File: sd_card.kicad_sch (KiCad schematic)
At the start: 19 parts, among them J5 Screw_Terminal_01x03, J601 DM3AT-SF-PEJM5_40_, U11 EMIF06-MSD02N16, U602 ADM2565EBRNZ

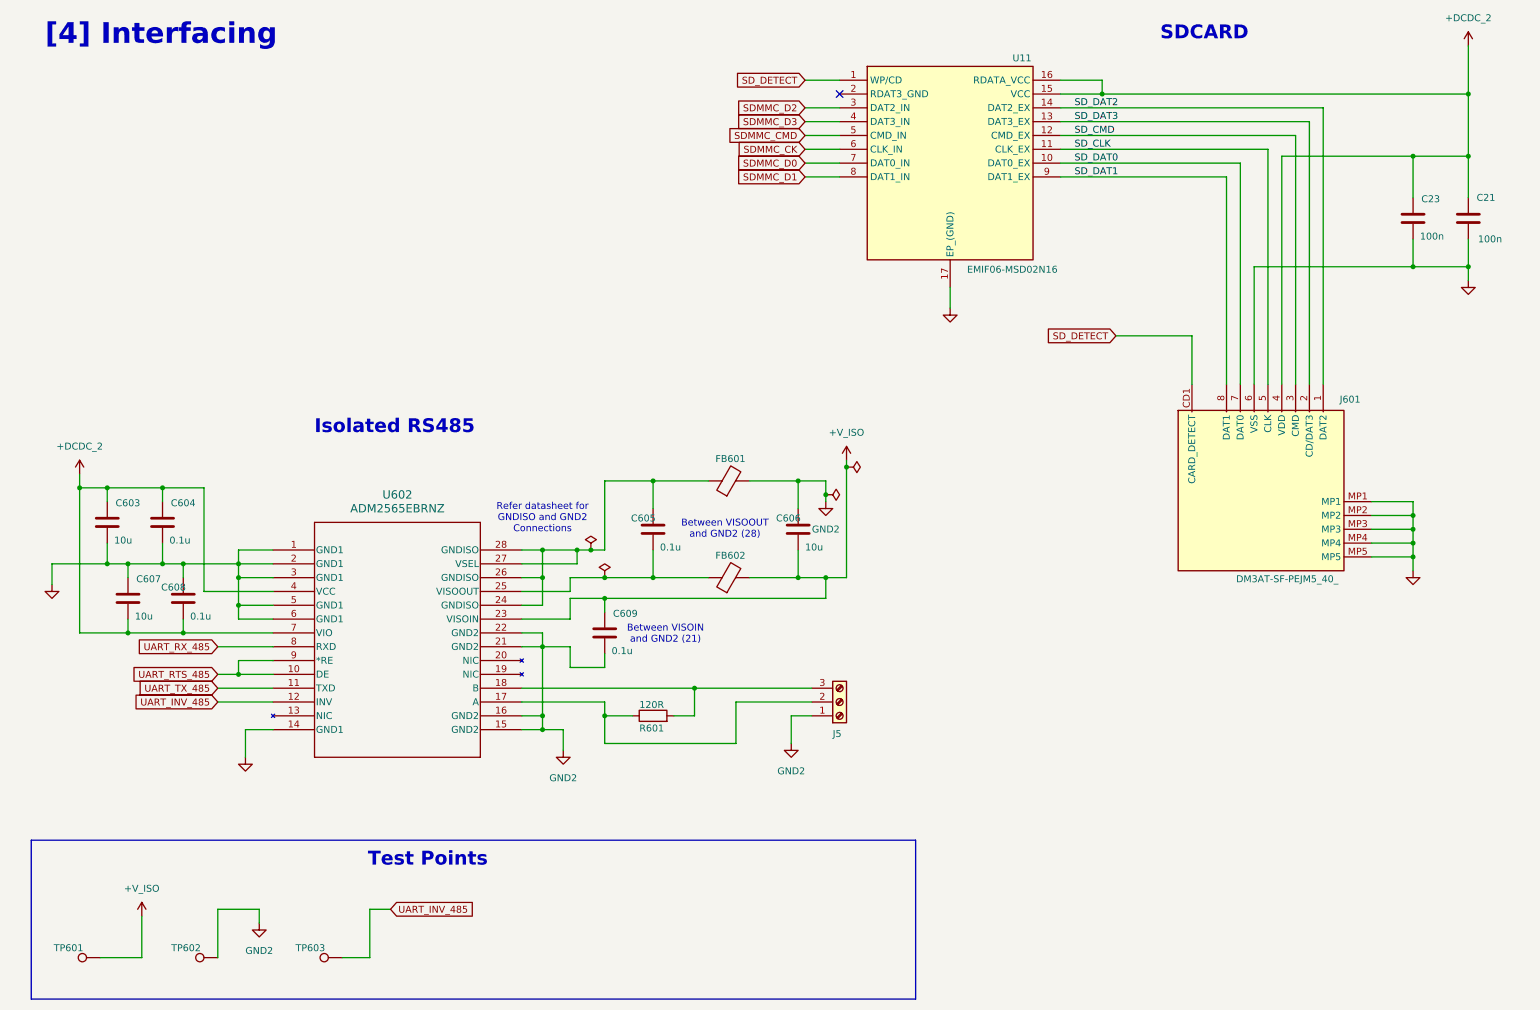
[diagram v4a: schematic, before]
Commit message: v2.0 schematics updated
1. Need to be tested for errors
2. PCB layout is not started yet
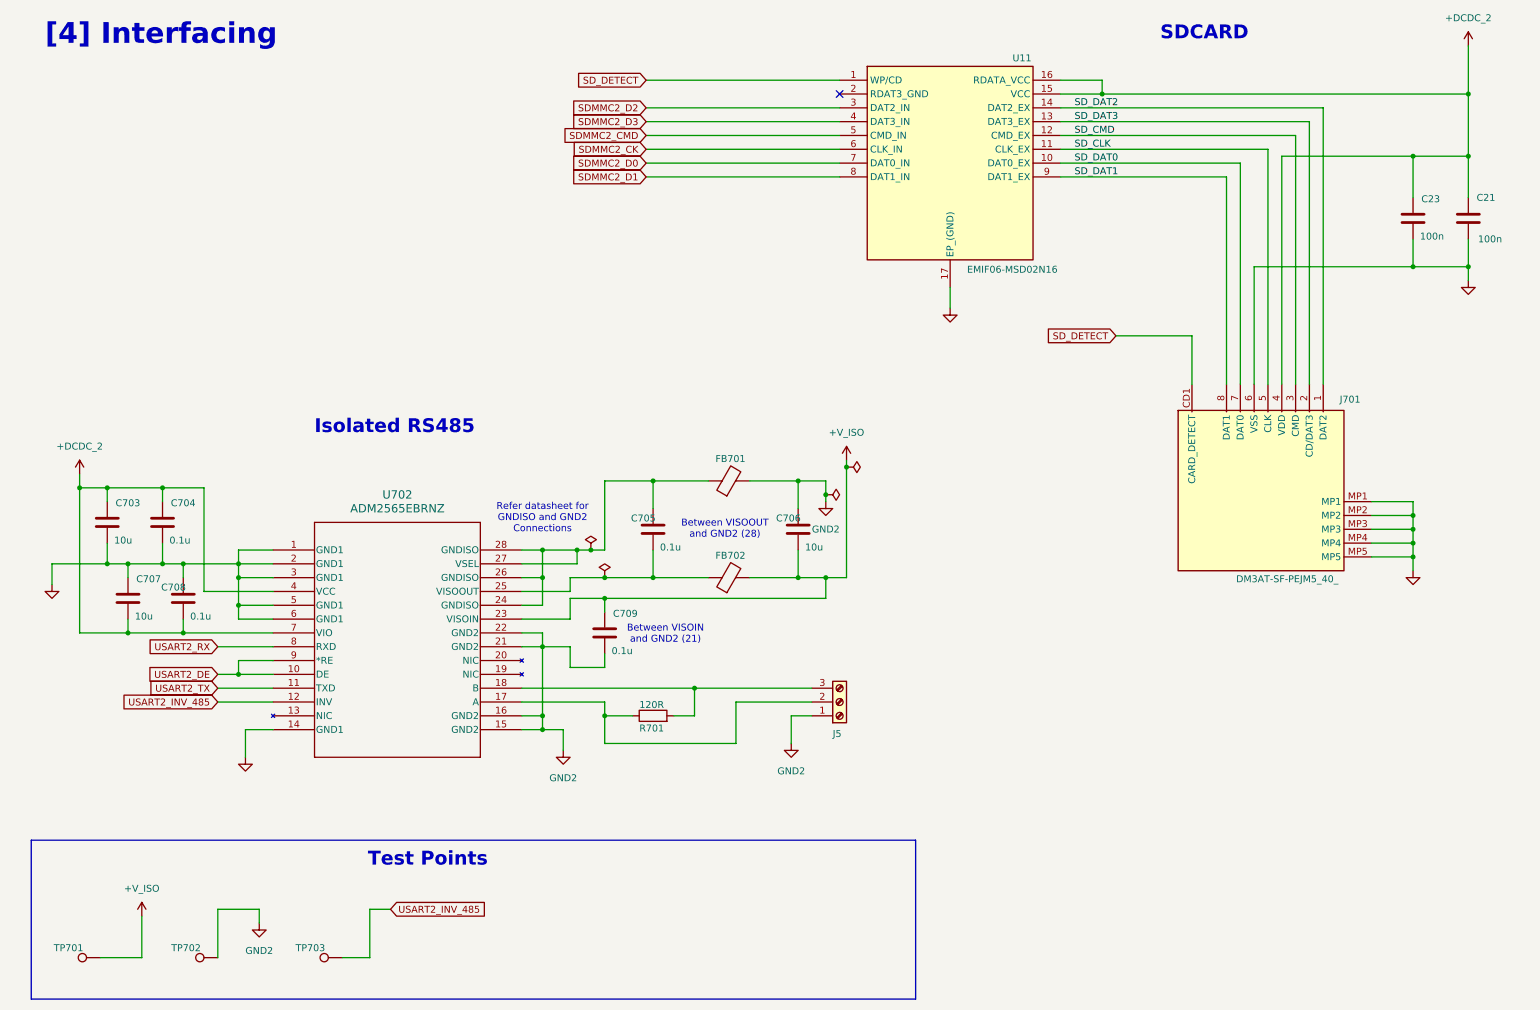
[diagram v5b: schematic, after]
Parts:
- renumbered C603 to C703, C604 to C704, C605 to C705, C606 to C706, C607 to C707, C608 to C708, C609 to C709, FB601 to FB701, FB602 to FB702, J601 to J701, R601 to R701, TP601 to TP701, TP602 to TP702, TP603 to TP703, U602 to U702
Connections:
- net SDMMC_CK renamed SDMMC2_CK
- net SDMMC_CMD renamed SDMMC2_CMD
- net SDMMC_D0 renamed SDMMC2_D0
- net SDMMC_D1 renamed SDMMC2_D1
- net SDMMC_D2 renamed SDMMC2_D2
- net SDMMC_D3 renamed SDMMC2_D3
- net UART_INV_485 renamed USART2_INV_485
- net UART_RTS_485 renamed USART2_DE
- net UART_RX_485 renamed USART2_RX
- net UART_TX_485 renamed USART2_TX

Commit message: minor formatting updates
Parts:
- TP701, TP702, TP703: footprint EMS:5000 -> TestPoint:TestPoint_Pad_D3.0mm
- renumbered C703 to C701, C707 to C702, C704 to C703, C708 to C704, C709 to C705, C705 to C706, C706 to C707, J701 to J702, U702 to U701
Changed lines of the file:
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@@
 		(on_board yes)
 		(dnp no)
-		(property "Reference" "C707"
+		(property "Reference" "C702"
 			(at 32.004 119.634 0)
 			(effects
@@
 			(project "EnergyMonitoringSystem"
 				(path "/e660428c-c9b7-476c-8ac8-2d419f233469/107b47ad-de26-4dce-b636-52b3b123a40b"
-					(reference "C707")
+					(reference "C702")
 					(unit 1)
 				)
@@
 		(dnp no)
 		(fields_autoplaced yes)
-		(property "Reference" "#PWR0707"
+		(property "Reference" "#PWR0711"
 			(at 266.7 124.46 0)
 			(effects
@@
 			(project "EnergyMonitoringSystem"
 				(path "/e660428c-c9b7-476c-8ac8-2d419f233469/107b47ad-de26-4dce-b636-52b3b123a40b"
-					(reference "#PWR0707")
+					(reference "#PWR0711")
 					(unit 1)
 				)
@@
 		(dnp no)
 		(fields_autoplaced yes)
-		(property "Reference" "U702"
+		(property "Reference" "U701"
 			(at 80.01 104.14 0)
 			(effects
@@
 			(project ""
 				(path "/e660428c-c9b7-476c-8ac8-2d419f233469/107b47ad-de26-4dce-b636-52b3b123a40b"
-					(reference "U702")
+					(reference "U701")
 					(unit 1)
 				)
@@
 			(project ""
 				(path "/e660428c-c9b7-476c-8ac8-2d419f233469/107b47ad-de26-4dce-b636-52b3b123a40b"
-					(reference "U701")
+					(reference "U702")
 					(unit 1)
 				)
@@
 		(on_board yes)
 		(dnp no)
-		(property "Reference" "C704"
+		(property "Reference" "C703"
 			(at 38.354 105.664 0)
 			(effects
@@
 			(project "EnergyMonitoringSystem"
 				(path "/e660428c-c9b7-476c-8ac8-2d419f233469/107b47ad-de26-4dce-b636-52b3b123a40b"
-					(reference "C704")
+					(reference "C703")
 					(unit 1)
 				)
@@
 		(dnp no)
 		(fields_autoplaced yes)
-		(property "Reference" "#FLG0703"
+		(property "Reference" "#FLG0701"
 			(at 115.57 112.395 0)
 			(effects
@@
 			(project "EnergyMonitoringSystem"
 				(path "/e660428c-c9b7-476c-8ac8-2d419f233469/107b47ad-de26-4dce-b636-52b3b123a40b"
-					(reference "#FLG0703")
+					(reference "#FLG0701")
 					(unit 1)
 				)
@@
 			)
 		)
-		(property "Footprint" "EMS:5000"
+		(property "Footprint" "TestPoint:TestPoint_Pad_D3.0mm"
 			(at 46.99 184.15 0)
 			(effects
@@
 			(project ""
 				(path "/e660428c-c9b7-476c-8ac8-2d419f233469/107b47ad-de26-4dce-b636-52b3b123a40b"
-					(reference "C702")
+					(reference "C709")
 					(unit 1)
 				)
@@
 		(dnp no)
 		(fields_autoplaced yes)
-		(property "Reference" "#PWR0711"
+		(property "Reference" "#PWR0704"
 			(at 52.07 158.75 0)
 			(effects
@@
 			(project "EnergyMonitoringSystem"
 				(path "/e660428c-c9b7-476c-8ac8-2d419f233469/107b47ad-de26-4dce-b636-52b3b123a40b"
-					(reference "#PWR0711")
+					(reference "#PWR0704")
 					(unit 1)
 				)
@@
 		(dnp no)
 		(fields_autoplaced yes)
-		(property "Reference" "#PWR0710"
+		(property "Reference" "#PWR0706"
 			(at 110.49 157.48 0)
 			(effects
@@
 			(project "EnergyMonitoringSystem"
 				(path "/e660428c-c9b7-476c-8ac8-2d419f233469/107b47ad-de26-4dce-b636-52b3b123a40b"
-					(reference "#PWR0710")
+					(reference "#PWR0706")
 					(unit 1)
 				)
@@
 		(dnp no)
 		(fields_autoplaced yes)
-		(property "Reference" "#PWR0706"
+		(property "Reference" "#PWR0708"
 			(at 158.75 111.76 0)
 			(effects
@@
 			(project ""
 				(path "/e660428c-c9b7-476c-8ac8-2d419f233469/107b47ad-de26-4dce-b636-52b3b123a40b"
-					(reference "#PWR0706")
+					(reference "#PWR0708")
 					(unit 1)
 				)
@@
 		(on_board yes)
 		(dnp no)
-		(property "Reference" "C708"
+		(property "Reference" "C704"
 			(at 36.576 121.158 0)
 			(effects
@@
 			(project "EnergyMonitoringSystem"
 				(path "/e660428c-c9b7-476c-8ac8-2d419f233469/107b47ad-de26-4dce-b636-52b3b123a40b"
-					(reference "C708")
+					(reference "C704")
 					(unit 1)
 				)
@@
 		(on_board yes)
 		(dnp no)
-		(property "Reference" "C706"
+		(property "Reference" "C707"
 			(at 149.606 108.458 0)
 			(effects
@@
 			(project "EnergyMonitoringSystem"
 				(path "/e660428c-c9b7-476c-8ac8-2d419f233469/107b47ad-de26-4dce-b636-52b3b123a40b"
-					(reference "C706")
+					(reference "C707")
 					(unit 1)
 				)
@@
 		(on_board yes)
 		(dnp no)
-		(property "Reference" "C703"
+		(property "Reference" "C701"
 			(at 28.194 105.664 0)
 			(effects
@@
 			(project "EnergyMonitoringSystem"
 				(path "/e660428c-c9b7-476c-8ac8-2d419f233469/107b47ad-de26-4dce-b636-52b3b123a40b"
-					(reference "C703")
+					(reference "C701")
 					(unit 1)
 				)
@@
 		(dnp no)
 		(fields_autoplaced yes)
-		(property "Reference" "#PWR0713"
+		(property "Reference" "#PWR0705"
 			(at 54.61 189.23 0)
 			(effects
@@
 			(project "EnergyMonitoringSystem"
 				(path "/e660428c-c9b7-476c-8ac8-2d419f233469/107b47ad-de26-4dce-b636-52b3b123a40b"
-					(reference "#PWR0713")
+					(reference "#PWR0705")
 					(unit 1)
 				)
@@
 			(project ""
 				(path "/e660428c-c9b7-476c-8ac8-2d419f233469/107b47ad-de26-4dce-b636-52b3b123a40b"
-					(reference "#PWR0702")
+					(reference "#PWR0713")
 					(unit 1)
 				)
@@
 		(dnp no)
 		(fields_autoplaced yes)
-		(property "Reference" "#FLG0704"
+		(property "Reference" "#FLG0702"
 			(at 118.11 117.475 0)
 			(effects
@@
 			(project "EnergyMonitoringSystem"
 				(path "/e660428c-c9b7-476c-8ac8-2d419f233469/107b47ad-de26-4dce-b636-52b3b123a40b"
-					(reference "#FLG0704")
+					(reference "#FLG0702")
 					(unit 1)
 				)
@@
 		(dnp no)
 		(fields_autoplaced yes)
-		(property "Reference" "#PWR0712"
+		(property "Reference" "#PWR0703"
 			(at 37.592 180.848 0)
 			(effects
@@
 			(project "EnergyMonitoringSystem"
 				(path "/e660428c-c9b7-476c-8ac8-2d419f233469/107b47ad-de26-4dce-b636-52b3b123a40b"
-					(reference "#PWR0712")
+					(reference "#PWR0703")
 					(unit 1)
 				)
@@
 		(dnp no)
 		(fields_autoplaced yes)
-		(property "Reference" "#FLG0702"
+		(property "Reference" "#FLG0703"
 			(at 160.655 104.14 0)
 			(effects
@@
 			(project "EnergyMonitoringSystem"
 				(path "/e660428c-c9b7-476c-8ac8-2d419f233469/107b47ad-de26-4dce-b636-52b3b123a40b"
-					(reference "#FLG0702")
+					(reference "#FLG0703")
 					(unit 1)
 				)
@@
 		(on_board yes)
 		(dnp no)
-		(property "Reference" "J701"
+		(property "Reference" "J702"
 			(at 257.048 86.614 0)
 			(effects
@@
 			(project ""
 				(path "/e660428c-c9b7-476c-8ac8-2d419f233469/107b47ad-de26-4dce-b636-52b3b123a40b"
-					(reference "J701")
+					(reference "J702")
 					(unit 1)
 				)
@@
 			)
 		)
-		(property "Footprint" "EMS:5000"
+		(property "Footprint" "TestPoint:TestPoint_Pad_D3.0mm"
 			(at 25.4 184.15 0)
 			(effects
@@
 		(dnp no)
 		(fields_autoplaced yes)
-		(property "Reference" "#PWR0701"
+		(property "Reference" "#PWR0712"
 			(at 276.86 21.59 0)
 			(effects
@@
 			(project "EnergyMonitoringSystem"
 				(path "/e660428c-c9b7-476c-8ac8-2d419f233469/107b47ad-de26-4dce-b636-52b3b123a40b"
-					(reference "#PWR0701")
+					(reference "#PWR0712")
 					(unit 1)
 				)
@@
 		(on_board yes)
 		(dnp no)
-		(property "Reference" "C709"
+		(property "Reference" "C705"
 			(at 119.634 125.984 0)
 			(effects
@@
 			(project "EnergyMonitoringSystem"
 				(path "/e660428c-c9b7-476c-8ac8-2d419f233469/107b47ad-de26-4dce-b636-52b3b123a40b"
-					(reference "C709")
+					(reference "C705")
 					(unit 1)
 				)
@@
 			)
 		)
-		(property "Footprint" "EMS:5000"
+		(property "Footprint" "TestPoint:TestPoint_Pad_D3.0mm"
 			(at 69.85 184.15 0)
 			(effects
@@
 		(dnp no)
 		(fields_autoplaced yes)
-		(property "Reference" "#PWR0708"
+		(property "Reference" "#PWR0701"
 			(at 16.51 127 0)
 			(effects
@@
 			(project "EnergyMonitoringSystem"
 				(path "/e660428c-c9b7-476c-8ac8-2d419f233469/107b47ad-de26-4dce-b636-52b3b123a40b"
-					(reference "#PWR0708")
+					(reference "#PWR0701")
 					(unit 1)
 				)
@@
 		(dnp no)
 		(fields_autoplaced yes)
-		(property "Reference" "#PWR0709"
+		(property "Reference" "#PWR0707"
 			(at 152.4 156.21 0)
 			(effects
@@
 			(project "EnergyMonitoringSystem"
 				(path "/e660428c-c9b7-476c-8ac8-2d419f233469/107b47ad-de26-4dce-b636-52b3b123a40b"
-					(reference "#PWR0709")
+					(reference "#PWR0707")
 					(unit 1)
 				)
@@
 		(on_board yes)
 		(dnp no)
-		(property "Reference" "C705"
+		(property "Reference" "C706"
 			(at 122.936 108.458 0)
 			(effects
@@
 			(project "EnergyMonitoringSystem"
 				(path "/e660428c-c9b7-476c-8ac8-2d419f233469/107b47ad-de26-4dce-b636-52b3b123a40b"
-					(reference "C705")
+					(reference "C706")
 					(unit 1)
 				)
@@
 		(dnp no)
 		(fields_autoplaced yes)
-		(property "Reference" "#PWR0705"
+		(property "Reference" "#PWR0702"
 			(at 21.59 100.33 0)
 			(effects
@@
 			(project "EnergyMonitoringSystem"
 				(path "/e660428c-c9b7-476c-8ac8-2d419f233469/107b47ad-de26-4dce-b636-52b3b123a40b"
-					(reference "#PWR0705")
+					(reference "#PWR0702")
 					(unit 1)
 				)
@@
 			(project ""
 				(path "/e660428c-c9b7-476c-8ac8-2d419f233469/107b47ad-de26-4dce-b636-52b3b123a40b"
-					(reference "#PWR0703")
+					(reference "#PWR0710")
 					(unit 1)
 				)
@@
 			(project ""
 				(path "/e660428c-c9b7-476c-8ac8-2d419f233469/107b47ad-de26-4dce-b636-52b3b123a40b"
-					(reference "C701")
+					(reference "C708")
 					(unit 1)
 				)
@@
 		(dnp no)
 		(fields_autoplaced yes)
-		(property "Reference" "#FLG0701"
+		(property "Reference" "#FLG0704"
 			(at 164.465 99.06 0)
 			(effects
@@
 			(project "EnergyMonitoringSystem"
 				(path "/e660428c-c9b7-476c-8ac8-2d419f233469/107b47ad-de26-4dce-b636-52b3b123a40b"
-					(reference "#FLG0701")
+					(reference "#FLG0704")
 					(unit 1)
 				)
@@
 			(project ""
 				(path "/e660428c-c9b7-476c-8ac8-2d419f233469/107b47ad-de26-4dce-b636-52b3b123a40b"
-					(reference "J702")
+					(reference "J701")
 					(unit 1)
 				)
@@
 		(dnp no)
 		(fields_autoplaced yes)
-		(property "Reference" "#PWR0704"
+		(property "Reference" "#PWR0709"
 			(at 167.132 97.028 0)
 			(effects
@@
 			(project ""
 				(path "/e660428c-c9b7-476c-8ac8-2d419f233469/107b47ad-de26-4dce-b636-52b3b123a40b"
-					(reference "#PWR0704")
+					(reference "#PWR0709")
 					(unit 1)
 				)
